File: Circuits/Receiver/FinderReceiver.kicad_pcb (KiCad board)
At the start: 2 copper layers, 50 x 28 mm, 10 parts, among them P1 WRITER, U1 TWE_LITE_SMD

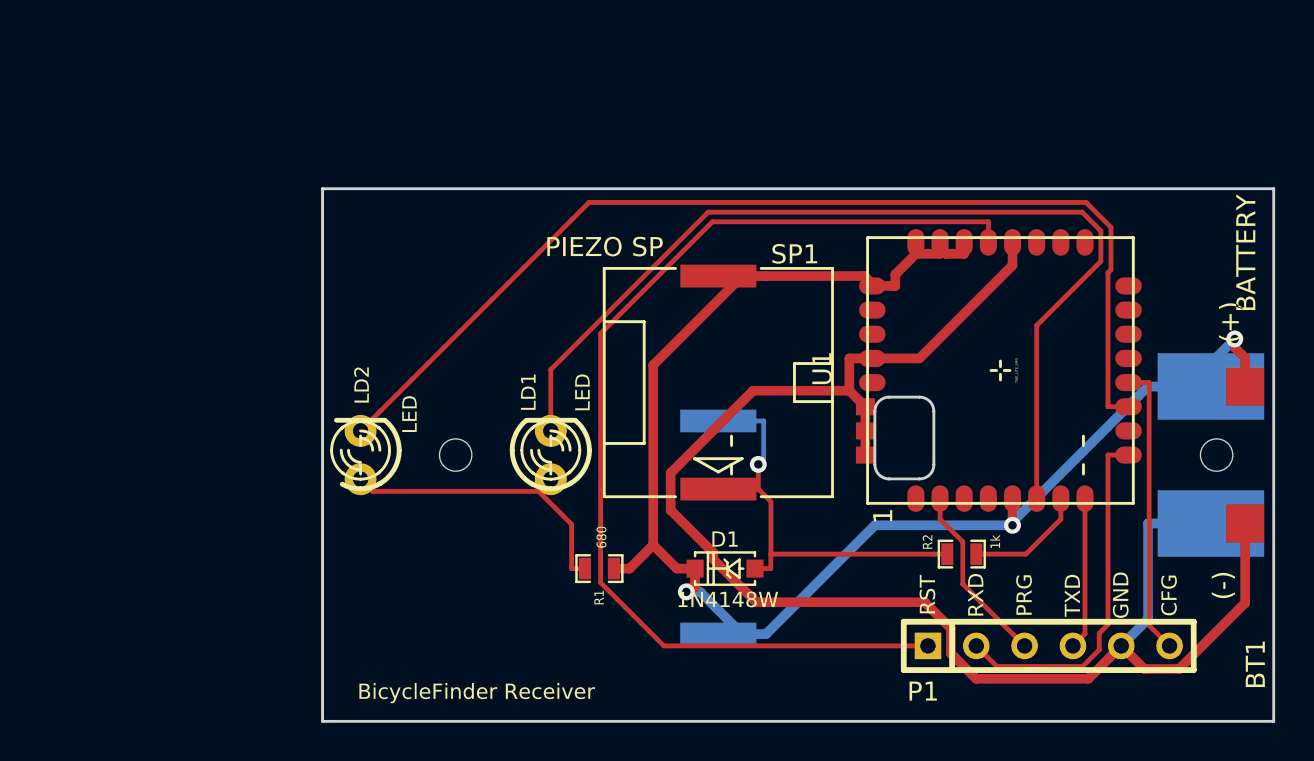
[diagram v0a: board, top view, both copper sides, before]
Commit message: Removed piezo speaker on front side.
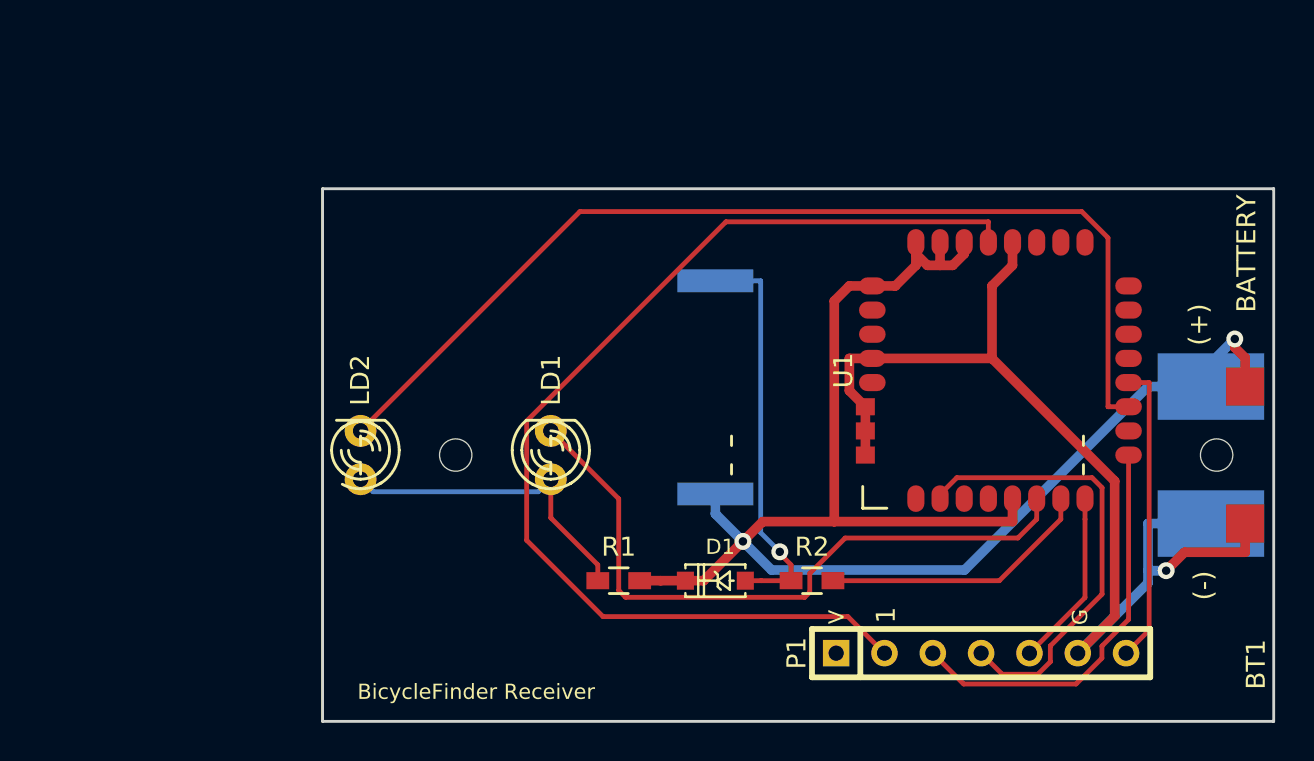
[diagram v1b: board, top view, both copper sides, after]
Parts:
- removed the SP1 at (49.7, 34.0)
- LD1: footprint LED-3MM -> LEDs:LED-3MM
- LD2: footprint LED-3MM -> favorites:LED-3MM
- P1: value WRITER -> WRITER-VCC; footprint WRITER-6P -> favorites:WRITE-7P
- R1, R2: footprint SM0603_Resistor -> Resistors_SMD:R_0603_HandSoldering
- SP1: renamed from SP2; footprint PIEZOSPK -> favorites:PIEZOSPK
- U1: footprint TWE-001L-NC7 -> favorites:TWE-001L-SMD-noNTH
- moved R2 8.00 mm to (54.6, 44.5)
- moved SP1 7.37 mm to (49.5, 34.3)
- moved P1 2.32 mm to (63.5, 48.3)
- moved R1 1.20 mm to (44.5, 44.5)
- moved D1 0.81 mm to (49.5, 44.5)
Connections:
- U1 pad 1: (no net) -> Net-(U1-Pad1)
- U1 pad 10: (no net) -> Net-(U1-Pad10)
- U1 pad 13: (no net) -> Net-(U1-Pad13)
- U1 pad 14: (no net) -> Net-(U1-Pad14)
- U1 pad 15: (no net) -> Net-(U1-Pad15)
- U1 pad 16: (no net) -> Net-(U1-Pad16)
- U1 pad 17: (no net) -> Net-(U1-Pad17)
- U1 pad 18: (no net) -> Net-(U1-Pad18)
- U1 pad 19: (no net) -> Net-(U1-Pad19)
- U1 pad 26: (no net) -> Net-(U1-Pad26)
- U1 pad 27: (no net) -> Net-(U1-Pad27)
- U1 pad 29: (no net) -> Net-(U1-Pad29)
- U1 pad 3: (no net) -> Net-(U1-Pad3)
- U1 pad 4: (no net) -> Net-(U1-Pad4)
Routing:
- net GND: track 82.4 -> 57.1 mm, vias 0 -> 1
- net /DO3: track 51.4 -> 35.3 mm
- net /PRG: track 9.58 -> 24.0 mm
- net /SOUND: track 6.29 -> 14.4 mm
- net /RXD: track 18.8 -> 21.4 mm
- net /RST: track 55.6 -> 57.2 mm
- net /SPK: track 22.7 -> 21.2 mm
- net VCC: track 81.5 -> 82.9 mm, vias 3 -> 2
- net /TXD: track 8.01 -> 9.33 mm
- net /DO4: track 55.5 -> 54.6 mm
- net /LED: track 16.0 -> 16.9 mm

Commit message: Replaced to current footprint modules.
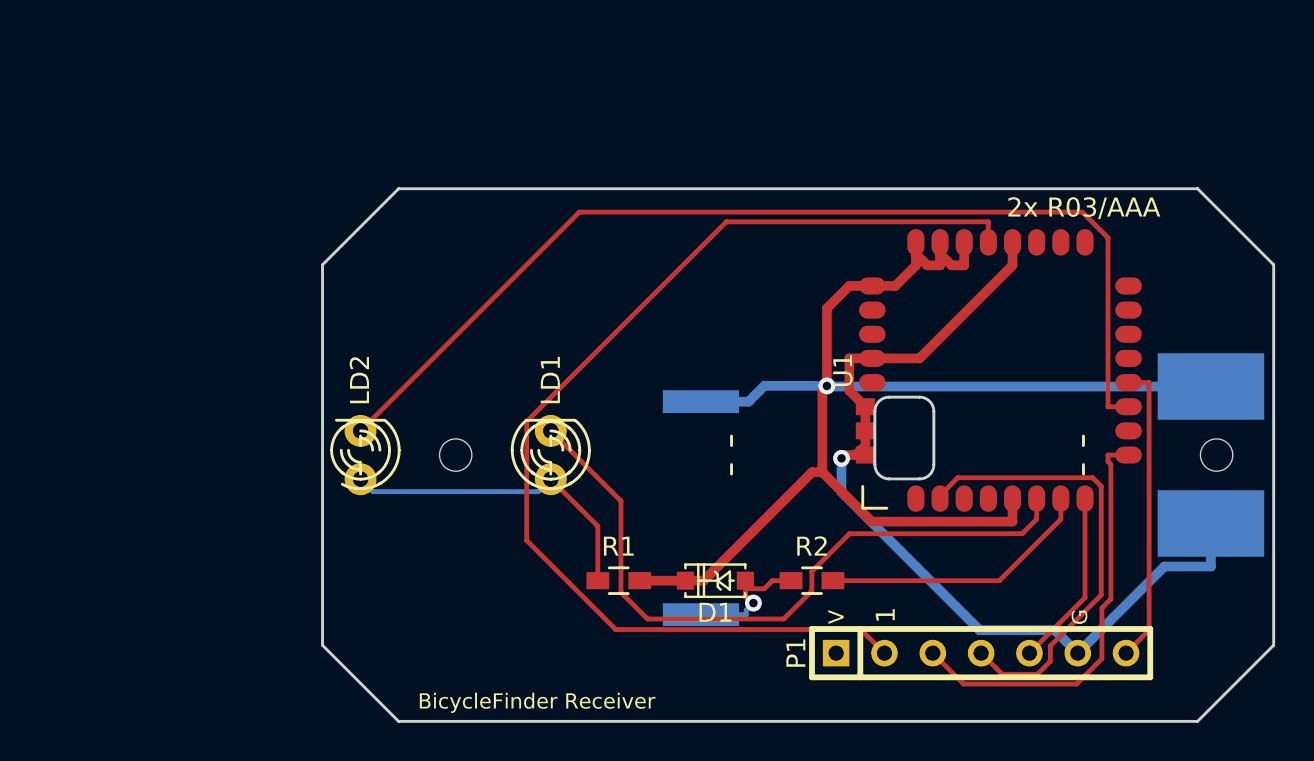
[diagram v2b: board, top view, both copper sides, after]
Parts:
- BT1: value BATTERY -> 2x R03/AAA; footprint FINDER_RECEIVER -> favorites:FINDER_RECEIVER
- D1: footprint SOD123 -> favorites:SOD123
- U1: footprint favorites:TWE-001L-SMD-noNTH -> favorites:TWE-001L-NC7
- moved SP1 6.40 mm to (48.8, 40.6), turned to 270 degrees
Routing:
- net /SPK: track 21.2 -> 7.15 mm
- net VCC: track 82.9 -> 72.4 mm, vias 2 -> 1
- net GND: track 57.1 -> 47.7 mm
- net /DO3: track 35.3 -> 36.3 mm
- net /RXD: track 21.4 -> 22.2 mm
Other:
- outline, holes or cut-outs redrawn

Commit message: Changed library file name from TWE-Lite to favorites. Added NJU72501MJE piezo speaker driver.
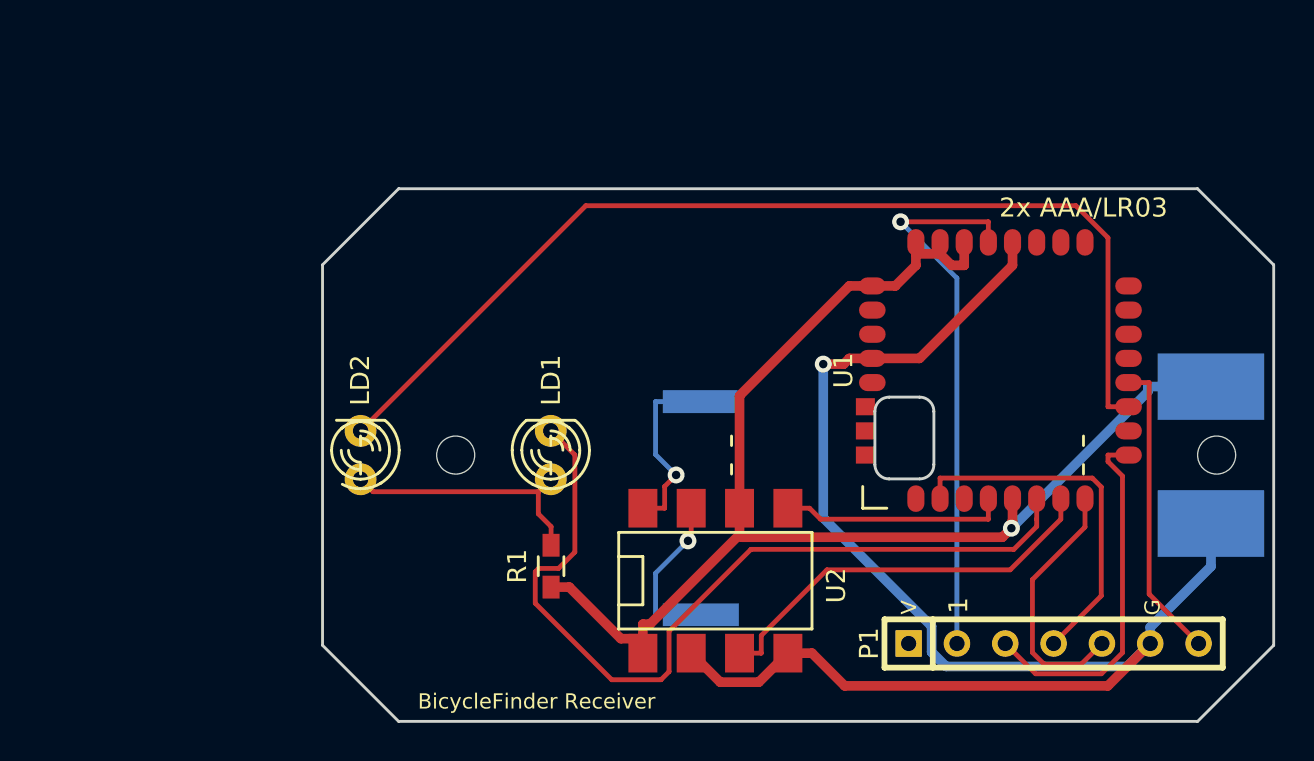
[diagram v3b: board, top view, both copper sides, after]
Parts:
- removed D1: 1N4148W, favorites:SOD123
- removed R2: 1k, Resistors_SMD:R_0603_HandSoldering
- added U2: NJU72501MJE, SMD_Packages:DIP-8_SMD, F.Cu at (49.5, 44.5)
- BT1: value 2x R03/AAA -> 2x AAA/LR03
- moved P1 3.84 mm to (67.3, 47.8)
- moved R1 3.64 mm to (40.9, 43.7), turned to 90 degrees
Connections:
- SP1 pad 1: VCC -> /VO1
- SP1 pad 2: /SPK -> /VO2
- U1 pad 30: GND -> Net-(U1-Pad30)
- U1 pad 31: GND -> Net-(U1-Pad31)
- U1 pad 32: GND -> Net-(U1-Pad32)
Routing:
- net GND: track 47.7 -> 77.8 mm
- net /RST: track 57.2 -> 29.1 mm, vias 0 -> 1
- net Net-(U1-Pad4): track 0.00 -> 11.9 mm
- net /VO1: track 0.00 -> 9.82 mm, vias 0 -> 1
- net /DO3: track 36.3 -> 45.1 mm
- net /VO2: track 0.00 -> 8.76 mm, vias 0 -> 1
- net /SPK: track 7.15 -> 0.00 mm, vias 1 -> 0
- net /SOUND: track 14.4 -> 21.4 mm
- net /PRG: track 23.9 -> 19.0 mm
- net /TXD: track 9.33 -> 13.6 mm
- net /LED: track 16.9 -> 13.6 mm
- net /RXD: track 22.2 -> 19.1 mm
- net VCC: track 72.4 -> 69.6 mm

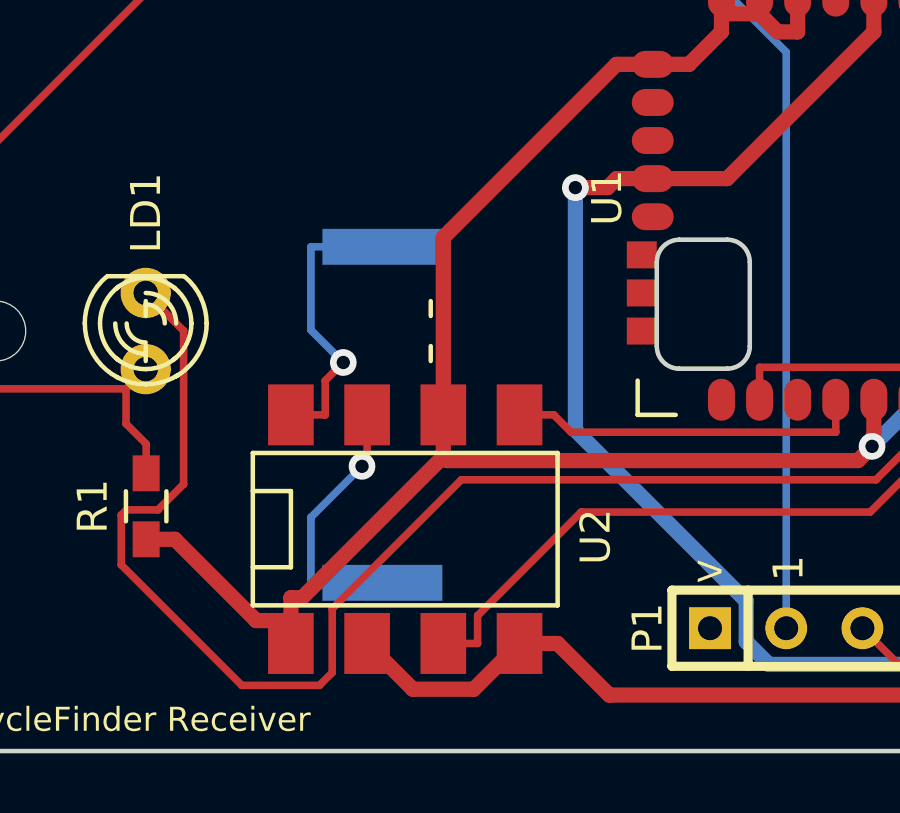
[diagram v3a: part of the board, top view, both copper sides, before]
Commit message: Control EN2 by DO2 GPIO instead of a jumper.
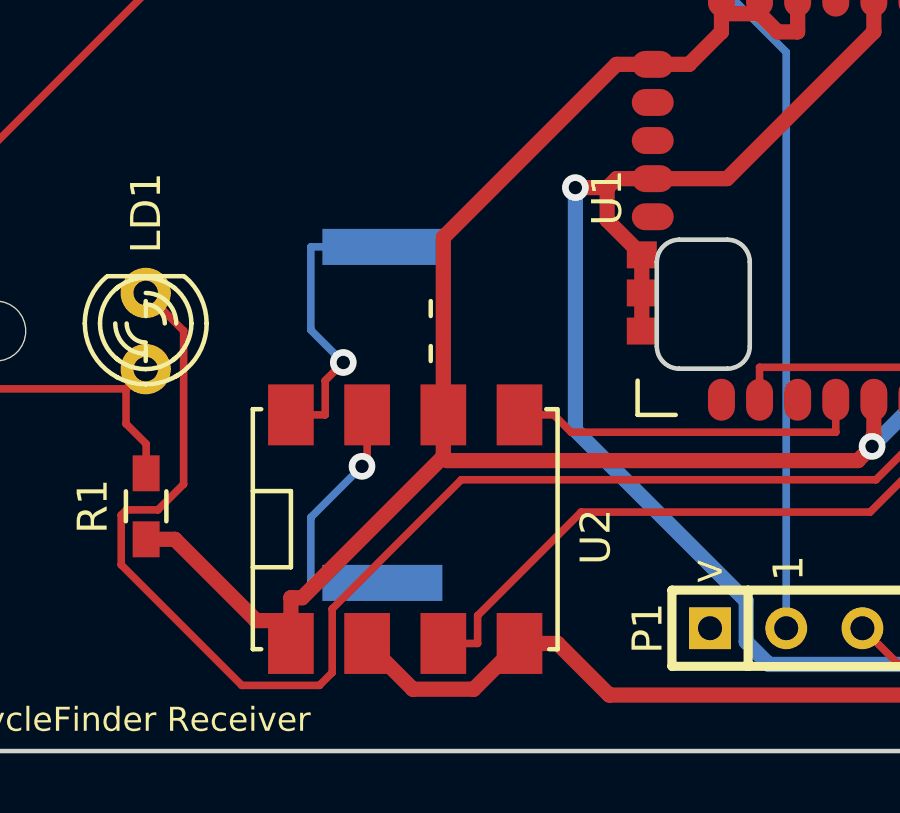
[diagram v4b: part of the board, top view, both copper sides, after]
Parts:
- U2: footprint SMD_Packages:DIP-8_SMD -> favorites:AE-NJU72501MJE
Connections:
- net Net-(U1-Pad4) renamed /EN2
- U1 pad 30: Net-(U1-Pad30) -> GND
- U1 pad 31: Net-(U1-Pad31) -> GND
- U1 pad 32: Net-(U1-Pad32) -> GND
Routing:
- net GND: track 77.8 -> 83.0 mm

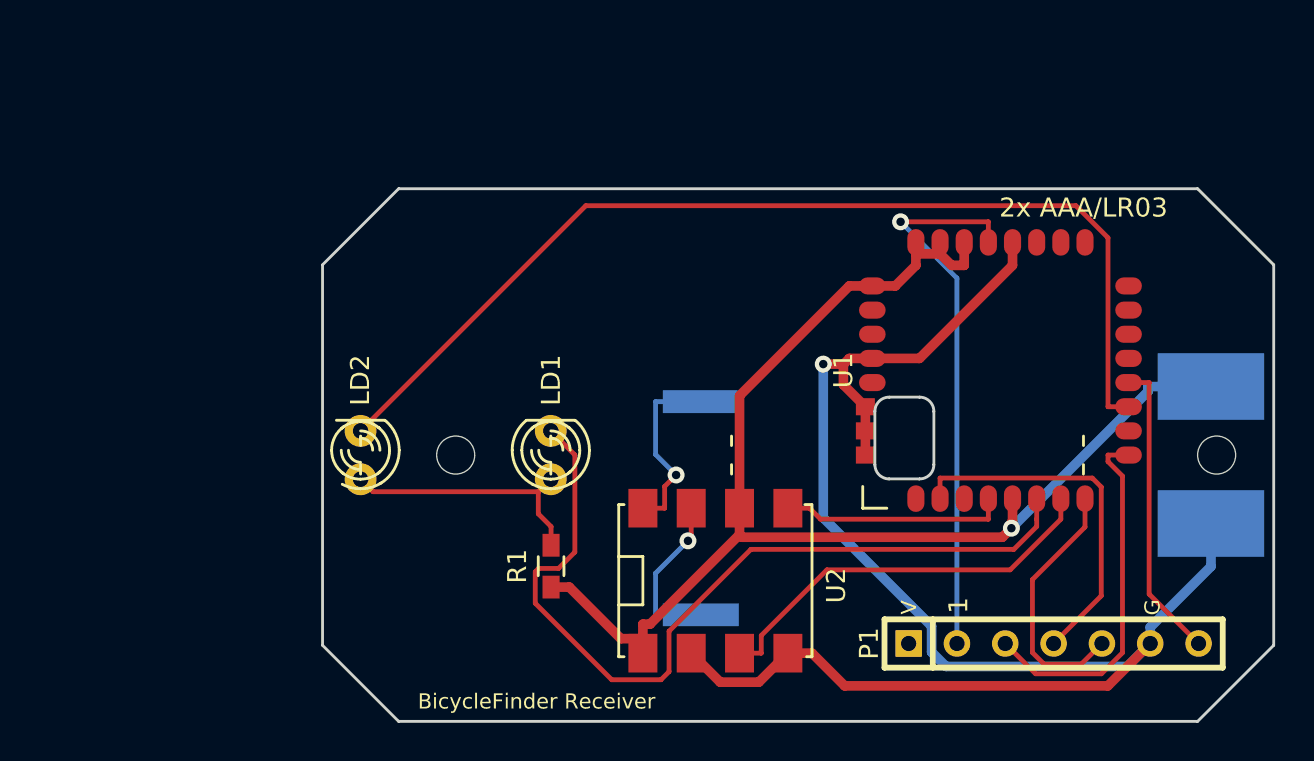
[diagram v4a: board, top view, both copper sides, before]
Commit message: Added RESET rubber switch.
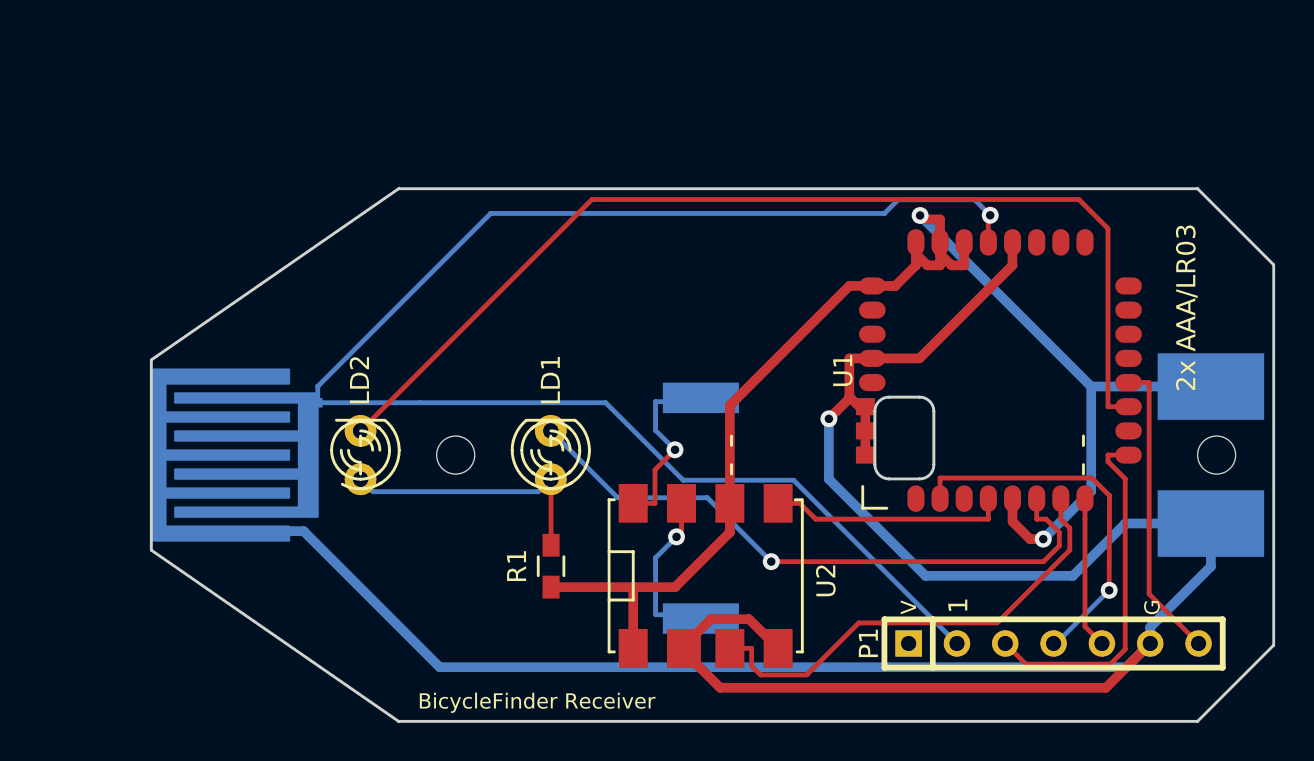
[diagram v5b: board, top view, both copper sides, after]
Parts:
- added SW1: SW_PUSH, favorites:RUBBER_SWITCH, B.Cu at (24.1, 37.8)
- moved U2 0.57 mm to (49.0, 44.2)
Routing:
- net /RST: track 29.1 -> 80.9 mm
- net GND: track 83.0 -> 134.8 mm
- net /DO3: track 45.1 -> 33.2 mm, vias 0 -> 1
- net /TXD: track 13.6 -> 7.98 mm
- net VCC: track 69.6 -> 73.6 mm, vias 1 -> 2
- net /SOUND: track 21.4 -> 24.6 mm
- net /EN2: track 11.9 -> 12.5 mm
- net /DO4: track 54.9 -> 55.4 mm
- net /PRG: track 19.0 -> 19.4 mm, vias 0 -> 1
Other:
- board size 50 x 28 mm -> 59 x 28 mm

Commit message: Replaced footprint of SMD register.
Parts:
- R1: footprint Resistors_SMD:R_0603_HandSoldering -> Resistors_SMD:R_0603
